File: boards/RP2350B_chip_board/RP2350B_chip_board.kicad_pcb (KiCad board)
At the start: 2 copper layers, 52 x 71.5 mm, 49 parts, among them J1 USB_B_Micro, J2 Conn_02x26_Odd_Even, J3 Conn_02x26_Odd_Even, J4 SM03B-SRSS-TB, SW1 SW_Push, SW2 SW_Push, U1 RP2350_80QFN, U2 NCP1117-3.3_SOT223, U3 W25Q128JVS, U4 DNF, Y1 ABM8-272-T3

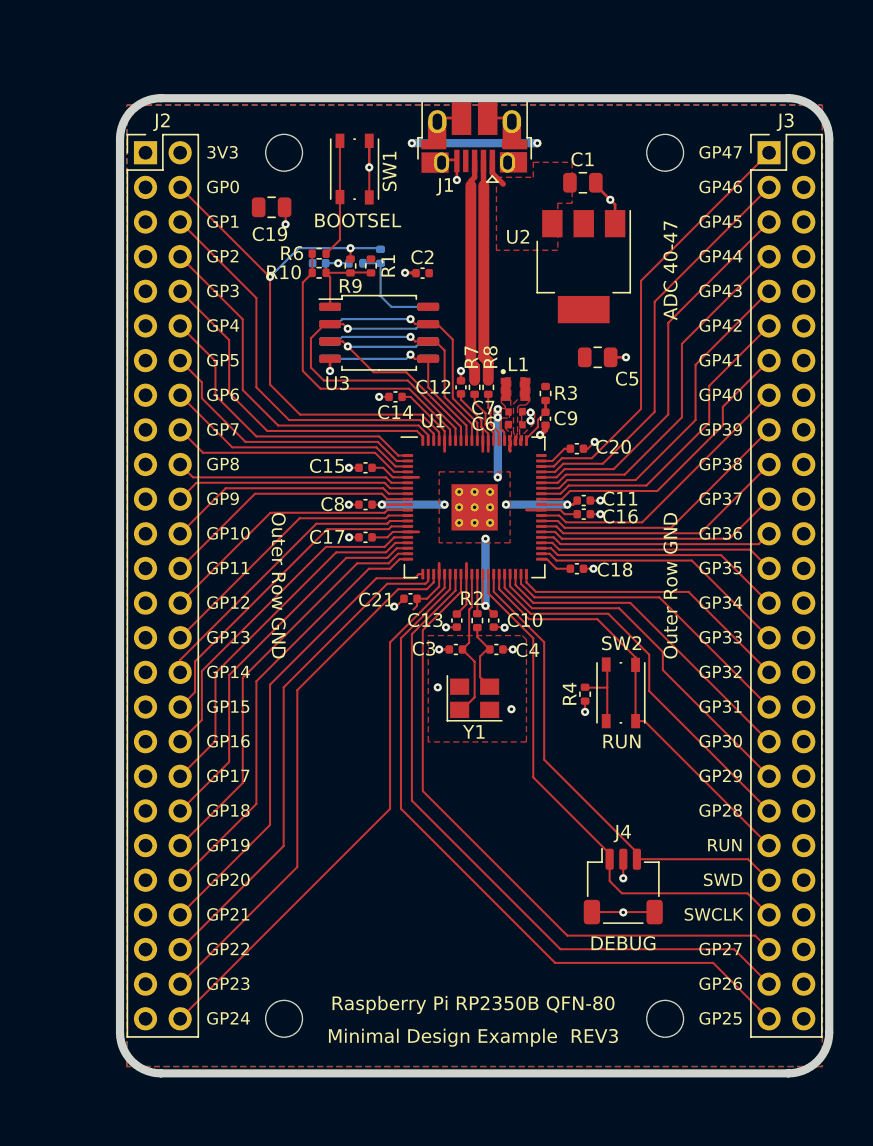
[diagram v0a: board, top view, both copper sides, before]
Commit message: Add Broker board
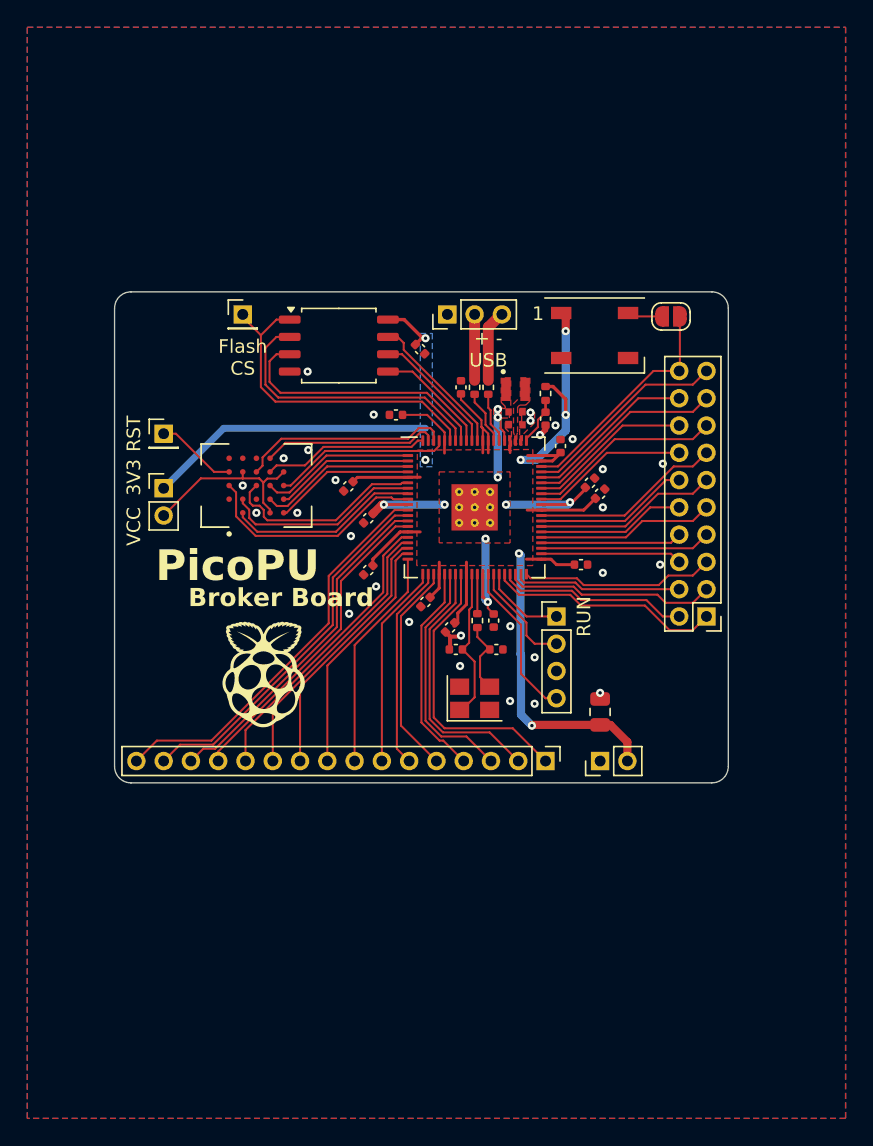
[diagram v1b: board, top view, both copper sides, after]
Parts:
- removed the C1 at (107.9, 76.2)
- removed the C19 at (85.1, 78.0)
- removed the C2 at (96.2, 82.8)
- removed C22: DNF, Capacitor_SMD:C_0402_1005Metric
- removed the C5 at (109.0, 89.0)
- removed H1, H2, H3, H4: MountingHole, MountingHole:MountingHole_2.7mm_M2.5
- removed the R1 at (92.4, 82.3)
- removed R10: 0, Resistor_SMD:R_0402_1005Metric
- removed R11, R13, R9: DNF, Resistor_SMD:R_0402_1005Metric
- removed the R4 at (108.1, 113.7)
- removed R6: 1k, Resistor_SMD:R_0402_1005Metric
- removed SW1, SW2: SW_Push, Button_Switch_SMD:SW_Push_1P1T_NO_Vertical_Wuerth_434133025816
- removed the U3 at (93.0, 87.2)
- removed U4: DNF, Package_SO:SOIC-8_5.23x5.23mm_P1.27mm
- added C16: 100n, Capacitor_SMD:C_0402_1005Metric, F.Cu at (96.0, 88.4)
- added C17: 10u, Capacitor_SMD:C_0805_2012Metric, F.Cu at (109.2, 115.0)
- added D1: WS2812B, LED_SMD:LED_WS2812B_PLCC4_5.0x5.0mm_P3.2mm, F.Cu at (108.8, 87.4)
- added J5: Conn_01x04, Connector_PinHeader_2.00mm:PinHeader_1x04_P2.00mm_Vertical, F.Cu at (106.0, 108.0)
- added J6: Conn_01x02, Connector_PinHeader_2.00mm:PinHeader_1x02_P2.00mm_Vertical, F.Cu at (109.2, 118.6)
- added J7: Conn_01x16, Connector_PinHeader_2.00mm:PinHeader_1x16_P2.00mm_Vertical, F.Cu at (105.2, 118.6)
- added J9: Conn_01x03, Connector_PinHeader_2.00mm:PinHeader_1x03_P2.00mm_Vertical, F.Cu at (98.0, 85.9)
- added JP1: SolderJumper_2_Open, Jumper:SolderJumper-2_P1.3mm_Open_RoundedPad1.0x1.5mm, F.Cu at (114.4, 86.0)
- added U1: IS66WVH8M8ALL-166B1LI, Custom:BGA25C100P5X5_800X600X120N, F.Cu at (84.0, 98.4)
- C14: renamed from C6; footprint RP2350_80QFN_minimal:C_0402_1005Metric_small_pads -> RP2350B_chip_board:C_0402_1005Metric_small_pads
- C15: renamed from C7; footprint RP2350_80QFN_minimal:C_0402_1005Metric_small_pads -> RP2350B_chip_board:C_0402_1005Metric_small_pads
- J1: value USB_B_Micro -> Conn_01x02; footprint Connector_USB:USB_Micro-B_Amphenol_10103594-0001LF_Horizontal -> Connector_PinHeader_2.00mm:PinHeader_1x02_P2.00mm_Vertical
- J2, J3: value Conn_02x26_Odd_Even -> Conn_01x01; footprint Connector_PinHeader_2.54mm:PinHeader_2x26_P2.54mm_Vertical -> Connector_PinHeader_2.00mm:PinHeader_1x01_P2.00mm_Vertical
- J4: value SM03B-SRSS-TB -> Conn_02x10_Odd_Even; footprint Connector_JST:JST_SH_SM03B-SRSS-TB_1x03-1MP_P1.00mm_Horizontal -> Connector_PinHeader_2.00mm:PinHeader_2x10_P2.00mm_Vertical
- L1: footprint RP2350_80QFN_minimal:L_pol_2016 -> RP2350B_chip_board:L_pol_2016
- U2: value NCP1117-3.3_SOT223 -> W25Q128JVS; footprint Package_TO_SOT_SMD:SOT-223-3_TabPin2 -> Package_SO:SOIC-8_5.23x5.23mm_P1.27mm
- U3: renamed from U1; footprint RP2350_80QFN_minimal:RP2350-QFN-80-1EP_10x10_P0.4mm_EP3.4x3.4mm_ThermalVias -> RP2350B_chip_board:RP2350-QFN-80-1EP_10x10_P0.4mm_EP3.4x3.4mm_ThermalVias
- moved J3 40.4 mm to (83.0, 85.9)
- moved J1 34.4 mm to (77.2, 98.6), turned to 0 degrees
- moved J4 20.7 mm to (117.0, 108.0), turned to 180 degrees
- moved J2 20.6 mm to (77.2, 94.6)
- moved U2 18.9 mm to (90.0, 88.1), turned to 0 degrees
- moved C9 2.41 mm to (92.2, 104.6), turned to -135 degrees
- moved C8 1.92 mm to (109.2, 99.0), turned to 45 degrees
- moved C7 1.85 mm to (90.7, 98.5), turned to -135 degrees
- moved C3 1.38 mm to (108.5, 98.2), turned to 45 degrees
- moved C6 1.32 mm to (94.2, 93.2)
- moved C11 1.22 mm to (106.3, 95.5), turned to 90 degrees
- moved C12 1.12 mm to (96.4, 106.9), turned to -135 degrees
- moved C1 1.02 mm to (92.2, 100.8), turned to -135 degrees
- moved C5 0.71 mm to (98.2, 108.8), turned to -135 degrees
- moved C10 0.42 mm to (107.8, 104.2)
- renumbered C8 to C1, C18 to C10, C20 to C11, C21 to C12, C9 to C13, C3 to C18, C4 to C19, C10 to C2, C11 to C3, C12 to C4, C13 to C5, C14 to C6, C15 to C7, C16 to C8, C17 to C9, R3 to R1, R7 to R2, R8 to R3, R2 to R4
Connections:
- J1 pad 1: VBUS -> +3V3
- J1 pad 2: /USB_D- -> Net-(J1-Pin_2)
- J2 pad 1: GND -> Net-(J2-Pin_1)
- J3 pad 1: /GPIO47_ADC7 -> /FLASH_SS
- J4 pad 1: /SWCLK -> /GPIO28
- J4 pad 2: GND -> /GPIO29
- J4 pad 3: /SWD -> /GPIO30
- U2 pad 1: GND -> /FLASH_SS
- U2 pad 2: +3V3 -> /QSPI_SD1
- U2 pad 3: VBUS -> /QSPI_SD2
- U3 pad 75: /QSPI_SS -> /FLASH_SS
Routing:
- net +3V3: track 52.9 -> 108.4 mm, vias 3 -> 7
- net GND: track 38.8 -> 3.16 mm
- net /GPIO25: track 52.1 -> 17.5 mm
- net /GPIO26: track 49.7 -> 19.2 mm
- net /GPIO0: track 41.5 -> 13.0 mm, vias 2 -> 0
- net /SWD: track 35.6 -> 7.95 mm
- net /SWCLK: track 38.9 -> 11.6 mm
- net /GPIO27: track 47.3 -> 20.9 mm
- net /RUN: track 31.4 -> 6.13 mm
- net /GPIO24: track 40.6 -> 16.1 mm
- net /GPIO23: track 39.0 -> 15.8 mm
- net /QSPI_SS: track 22.3 -> 0.00 mm
- net /GPIO22: track 36.7 -> 15.0 mm
- net /GPIO21: track 34.2 -> 14.9 mm
- net /FLASH_SS: track 5.96 -> 24.4 mm
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- added copper zone on B.Cu, net +3V3
- removed copper zone on F.Cu, net VBUS
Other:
- board size 52 x 71.5 mm -> 45 x 36 mm
- board text added: "+ - USB"
- board text added: "Broker Board"
- board text added: "Flash CS"
- board text added: "PicoPU"
- board text added: "RST"
- board text added: "VCC"
- board text removed: "ADC 40-47"
- board text removed: "BOOTSEL"
- board text removed: "DEBUG"
- board text removed: "GP0"
- board text removed: "GP1"
- board text removed: "GP10"
- board text removed: "GP11"
- board text removed: "GP12"
- board text removed: "GP13"
- board text removed: "GP14"
- board text removed: "GP15"
- board text removed: "GP16"
- board text removed: "GP17"
- board text removed: "GP18"
- board text removed: "GP19"
- board text removed: "GP2"
- board text removed: "GP20"
- board text removed: "GP21"
- board text removed: "GP22"
- board text removed: "GP23"
- board text removed: "GP24"
- board text removed: "GP25"
- board text removed: "GP26"
- board text removed: "GP27"
- board text removed: "GP28"
- board text removed: "GP29"
- board text removed: "GP3"
- board text removed: "GP30"
- board text removed: "GP31"
- board text removed: "GP32"
- board text removed: "GP33"
- board text removed: "GP34"
- board text removed: "GP35"
- board text removed: "GP36"
- board text removed: "GP37"
- board text removed: "GP38"
- board text removed: "GP39"
- board text removed: "GP4"
- board text removed: "GP40"
- board text removed: "GP41"
- board text removed: "GP42"
- board text removed: "GP43"
- board text removed: "GP44"
- board text removed: "GP45"
- board text removed: "GP46"
- board text removed: "GP47"
- board text removed: "GP5"
- board text removed: "GP6"
- board text removed: "GP7"
- board text removed: "GP8"
- board text removed: "GP9"
- board text removed: "Minimal Design Example REV3"
- board text removed: "Outer Row GND"
- board text removed: "Raspberry Pi RP2350B QFN-80"
- board text removed: "SWCLK"
- board text removed: "SWD"
